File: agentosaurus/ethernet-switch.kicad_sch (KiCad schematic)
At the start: 3 parts, among them T1 HX1188NL, U1 RTL8367S, Y1 25MHz

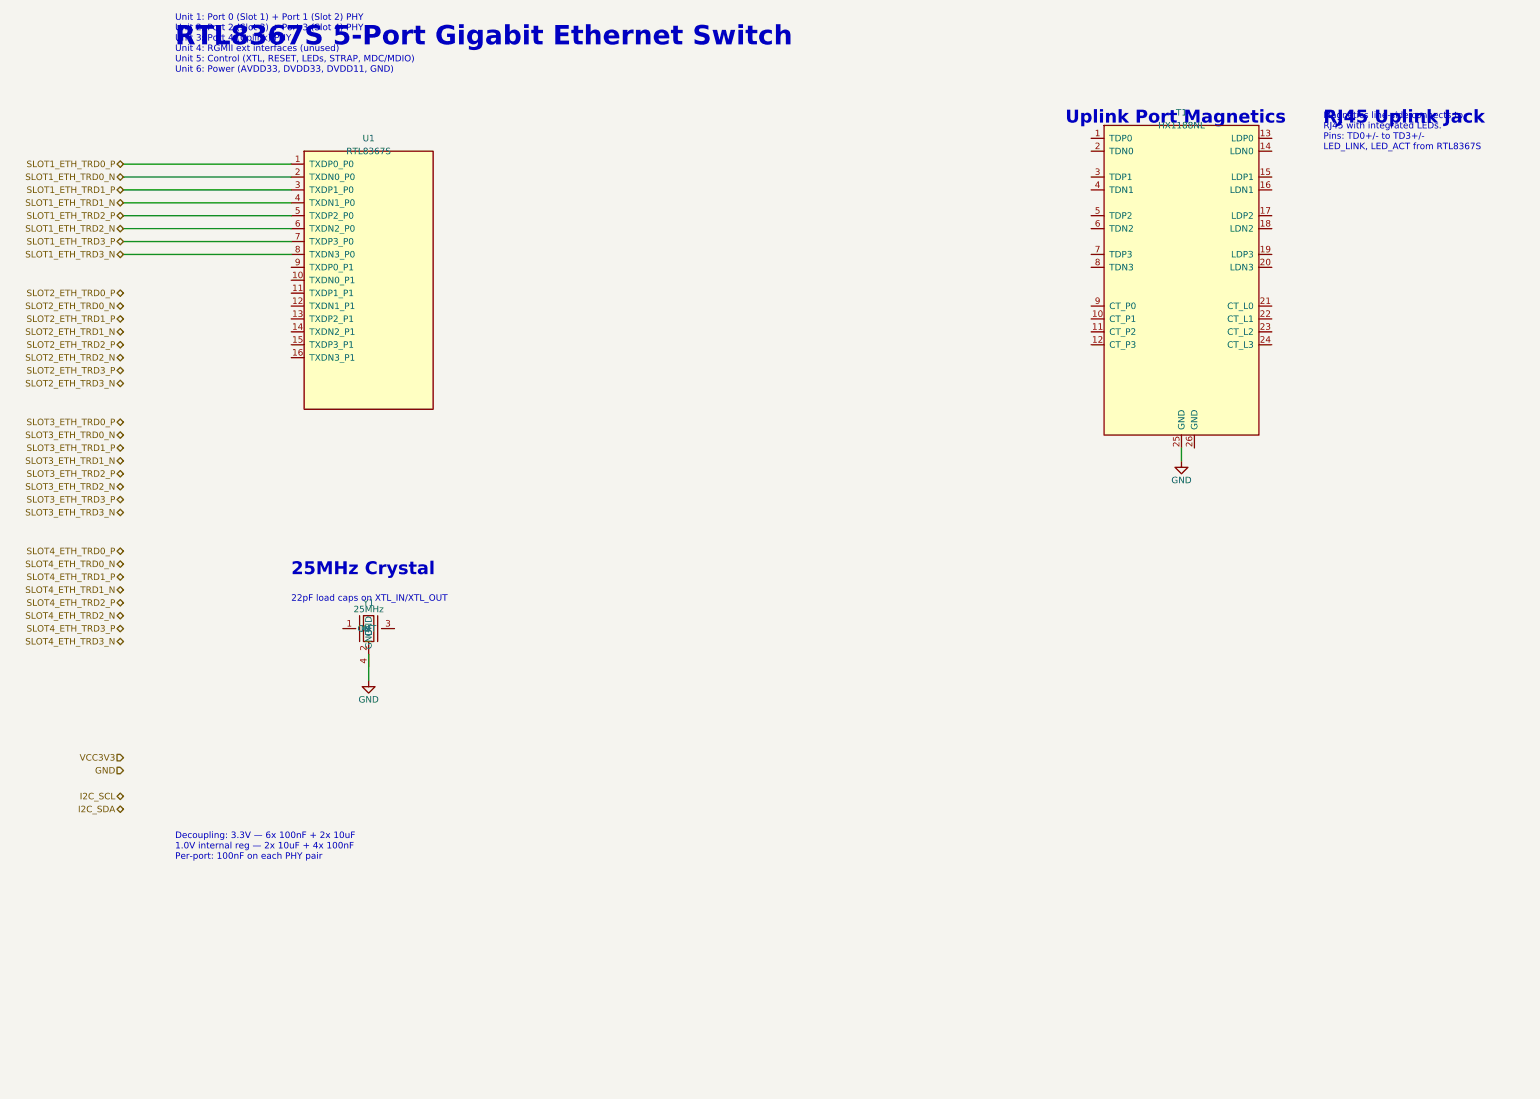
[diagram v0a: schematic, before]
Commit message: Add passive components to all schematic sheets
- power.kicad_sch: Fix D1 catch diode rotation (cathode→SW), remove
  incorrect COMP-to-output wire, add all TPS54360 application circuit
  passives (CIN1/2, CBOOT, L1, COUT1-3, R_EN1/2, R_RT, R_FB1/2,
  R_COMP, C_COMP) and AMS1117 caps (CIN_LDO, COUT_LDO)
- bmc.kicad_sch: Add USB-C CC pull-downs (R1/R2 5.1k), ESP32 reset
  circuit (R3 10k + C9 1uF), decoupling caps for ESP32 (C10/C11),
  UART mux (C12), USB mux (C13/C14), WS2812B (C15-C18), I2C
  pull-ups (R4/R5 4.7k)
- cm4-slot.kicad_sch: Add magnetics center-tap decoupling (C1-C4
  100nF) and power rail decoupling (C5-C8)
- ethernet-switch.kicad_sch: Add crystal load caps (C1/C2 22pF),
  3.3V decoupling (C3-C10), 1.0V core decoupling (C11-C16),
  Slot 2 Ethernet wiring to RTL8367S
- mechanical.kicad_sch: Add PCB stackup, impedance control, and
  via specifications

https://claude.ai/code/session_01UhhXLgEHsAy83XEALyNrDb
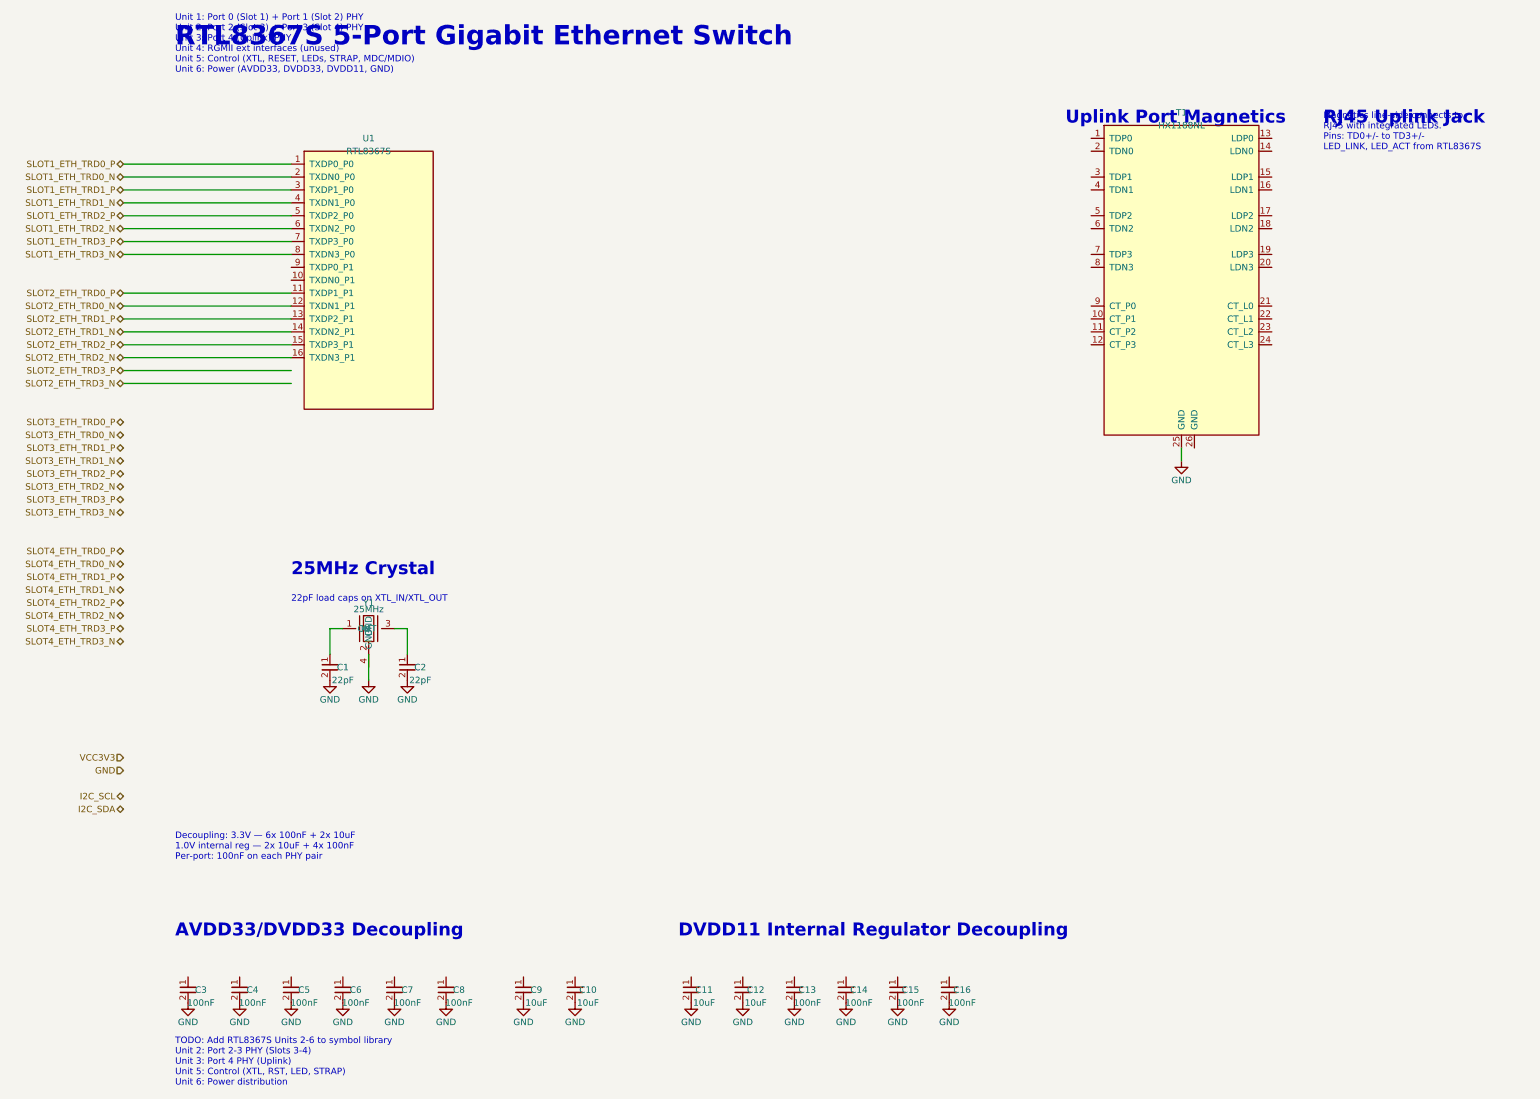
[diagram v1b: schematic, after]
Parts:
- added C1, C2: 22pF, Capacitor_SMD:C_0402_1005Metric, symbol Device:C
- added C10, C11, C12, C9: 10uF, Capacitor_SMD:C_0805_2012Metric, symbol Device:C
- added C13, C14, C15, C16, C3, C4, C5, C6, C7, C8: 100nF, Capacitor_SMD:C_0402_1005Metric, symbol Device:C
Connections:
- net GND: now also C1.2, C10.2, C11.2, C12.2, C13.2, C14.2, C15.2, C16.2, C2.2, C3.2, C4.2, C5.2, C6.2, C7.2, C8.2, C9.2
- net SLOT2_ETH_TRD0_N: now also U1.12 (TXDN1_P1)
- net SLOT2_ETH_TRD0_P: now also U1.11 (TXDP1_P1)
- net SLOT2_ETH_TRD1_N: now also U1.14 (TXDN2_P1)
- net SLOT2_ETH_TRD1_P: now also U1.13 (TXDP2_P1)
- net SLOT2_ETH_TRD2_N: now also U1.16 (TXDN3_P1)
- net SLOT2_ETH_TRD2_P: now also U1.15 (TXDP3_P1)
- net at Y1.1 (IN): now also C1.1
- net at Y1.3 (OUT): now also C2.1
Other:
- note added: "AVDD33/DVDD33 Decoupling"
- note added: "DVDD11 Internal Regulator Decoupling"
- note added: "TODO: Add RTL8367S Units 2-6 to symbol library Unit 2: Port 2-3 PHY (Slots 3-4) Unit 3: Port 4 PHY (Uplink) Unit 5: Control (XTL, RST, LED, STRAP) Unit 6: Power distribution"
